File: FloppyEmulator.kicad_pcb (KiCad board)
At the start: 2 copper layers, 69.9 x 48.3 mm, 48 parts, among them Q1 Crystal_GND24, Q2 BC817, Q3 BC817, SW1 ALPS_5WAY, U1 STM32F405RGTx, U10 AP1117-15, U2 SN74LVC2G07, U3 SN74LVC2G07, U4 SN74LVC2G07, U5 SN74LVC2G07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

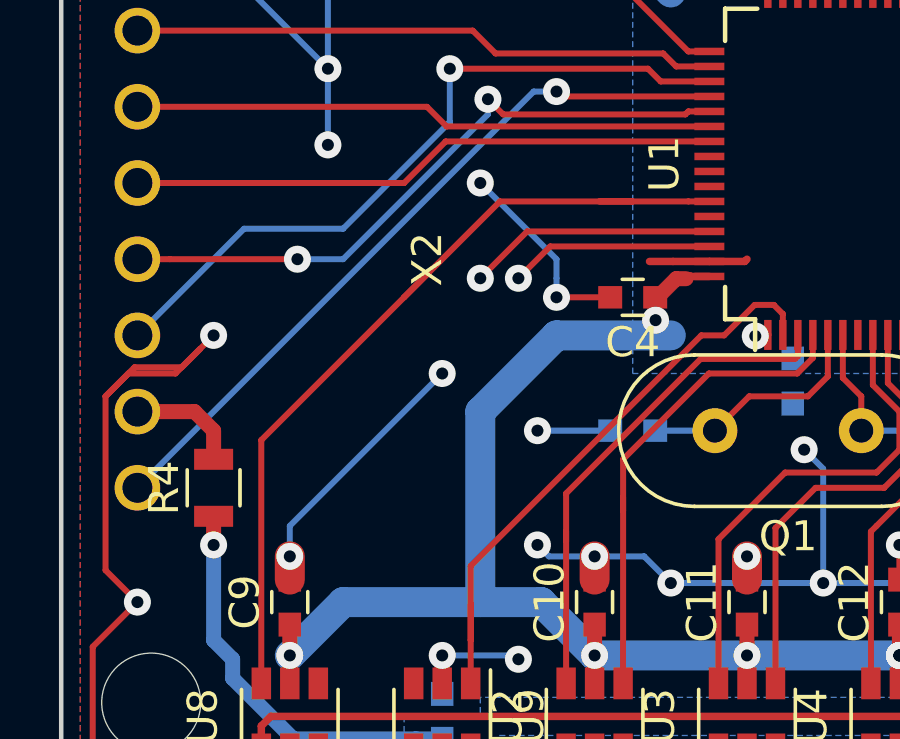
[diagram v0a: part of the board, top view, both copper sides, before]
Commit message: Add I2C pullups
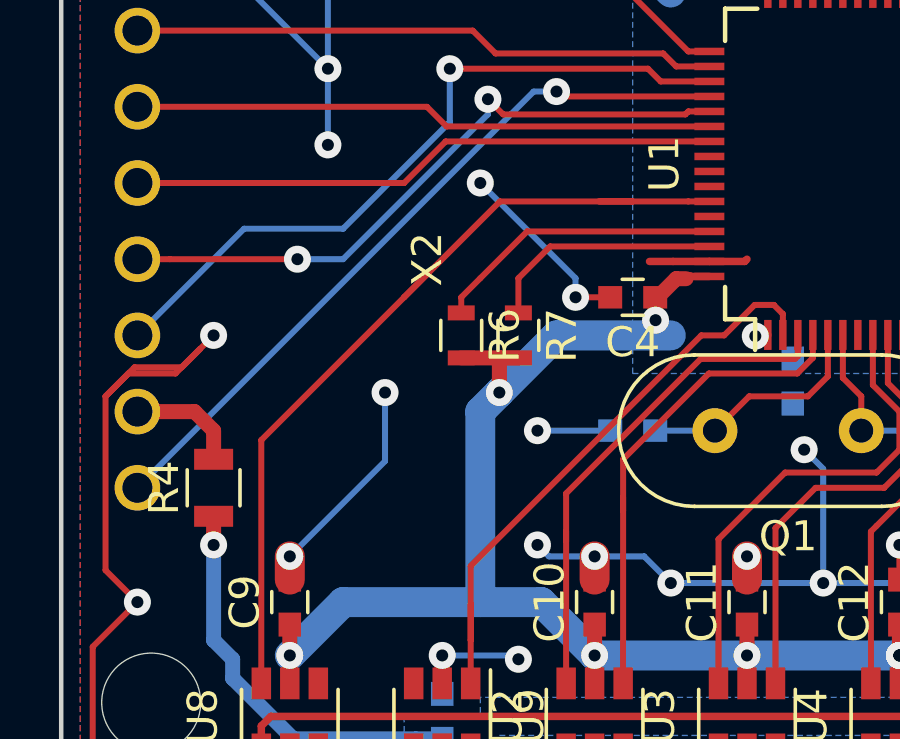
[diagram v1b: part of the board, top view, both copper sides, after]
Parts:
- added R6: DNF, Resistors_SMD:R_0603, F.Cu at (153.0, 82.5)
- added R7: DNF, Resistors_SMD:R_0603, F.Cu at (154.9, 82.5)
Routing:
- net +3V3: track 147.0 -> 150.1 mm, vias 24 -> 25
- net GND: track 374.6 -> 372.8 mm
- net SCL: track 8.28 -> 9.70 mm, vias 1 -> 0
- net SDA: track 6.80 -> 7.96 mm, vias 1 -> 0
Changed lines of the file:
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@@
     (thickness 1.6)
     (drawings 6)
-    (tracks 656)
+    (tracks 662)
     (zones 0)
-    (modules 48)
+    (modules 50)
     (nets 92)
   )
@@
   )
   (setup
-    (last_trace_width 0.2)
+    (last_trace_width 0.5)
     (user_trace_width 0.2)
     (user_trace_width 0.25)
@@
     )
   )
+  (module Resistors_SMD:R_0603 (layer F.Cu)
+    (at 153.035 82.55 270)
+    (descr "Resistor SMD 0603, reflow soldering, Vishay (see dcrcw.pdf)")
+    (tags "resistor 0603")
+    (attr smd)
+    (fp_text reference R6 (at 0 -1.45 270) (layer F.SilkS)
+      (effects (font (size 1 1) (thickness 0.15)))
+    )
+    (fp_text value DNF (at 0 1.5 270) (layer F.Fab)
+      (effects (font (size 1 1) (thickness 0.15)))
+    )
+    (fp_line (start 1.25 0.7) (end -1.25 0.7) (layer F.CrtYd) (width 0.05))
+    (fp_line (start 1.25 0.7) (end 1.25 -0.7) (layer F.CrtYd) (width 0.05))
+    (fp_line (start -1.25 -0.7) (end -1.25 0.7) (layer F.CrtYd) (width 0.05))
+    (fp_line (start -1.25 -0.7) (end 1.25 -0.7) (layer F.CrtYd) (width 0.05))
+    (fp_line (start -0.5 -0.68) (end 0.5 -0.68) (layer F.SilkS) (width 0.12))
+    (fp_line (start 0.5 0.68) (end -0.5 0.68) (layer F.SilkS) (width 0.12))
+    (fp_line (start -0.8 -0.4) (end 0.8 -0.4) (layer F.Fab) (width 0.1))
+    (fp_line (start 0.8 -0.4) (end 0.8 0.4) (layer F.Fab) (width 0.1))
+    (fp_line (start 0.8 0.4) (end -0.8 0.4) (layer F.Fab) (width 0.1))
+    (fp_line (start -0.8 0.4) (end -0.8 -0.4) (layer F.Fab) (width 0.1))
+    (fp_text user %R (at 0 0 270) (layer F.Fab)
+      (effects (font (size 0.4 0.4) (thickness 0.075)))
+    )
+    (pad 2 smd rect (at 0.75 0 270) (size 0.5 0.9) (layers F.Cu F.Paste F.Mask)
+      (net 9 +3V3))
+    (pad 1 smd rect (at -0.75 0 270) (size 0.5 0.9) (layers F.Cu F.Paste F.Mask)
+      (net 11 SCL))
+    (model ${KISYS3DMOD}/Resistors_SMD.3dshapes/R_0603.wrl
+      (at (xyz 0 0 0))
+      (scale (xyz 1 1 1))
+      (rotate (xyz 0 0 0))
+    )
+  )
+  (module Resistors_SMD:R_0603 (layer F.Cu)
+    (at 154.94 82.55 270)
+    (descr "Resistor SMD 0603, reflow soldering, Vishay (see dcrcw.pdf)")
+    (tags "resistor 0603")
+    (attr smd)
+    (fp_text reference R7 (at 0 -1.45 270) (layer F.SilkS)
+      (effects (font (size 1 1) (thickness 0.15)))
+    )
+    (fp_text value DNF (at 0 1.5 270) (layer F.Fab)
+      (effects (font (size 1 1) (thickness 0.15)))
+    )
+    (fp_text user %R (at 0 0 270) (layer F.Fab)
+      (effects (font (size 0.4 0.4) (thickness 0.075)))
+    )
+    (fp_line (start -0.8 0.4) (end -0.8 -0.4) (layer F.Fab) (width 0.1))
+    (fp_line (start 0.8 0.4) (end -0.8 0.4) (layer F.Fab) (width 0.1))
+    (fp_line (start 0.8 -0.4) (end 0.8 0.4) (layer F.Fab) (width 0.1))
+    (fp_line (start -0.8 -0.4) (end 0.8 -0.4) (layer F.Fab) (width 0.1))
+    (fp_line (start 0.5 0.68) (end -0.5 0.68) (layer F.SilkS) (width 0.12))
+    (fp_line (start -0.5 -0.68) (end 0.5 -0.68) (layer F.SilkS) (width 0.12))
+    (fp_line (start -1.25 -0.7) (end 1.25 -0.7) (layer F.CrtYd) (width 0.05))
+    (fp_line (start -1.25 -0.7) (end -1.25 0.7) (layer F.CrtYd) (width 0.05))
+    (fp_line (start 1.25 0.7) (end 1.25 -0.7) (layer F.CrtYd) (width 0.05))
+    (fp_line (start 1.25 0.7) (end -1.25 0.7) (layer F.CrtYd) (width 0.05))
+    (pad 1 smd rect (at -0.75 0 270) (size 0.5 0.9) (layers F.Cu F.Paste F.Mask)
+      (net 10 SDA))
+    (pad 2 smd rect (at 0.75 0 270) (size 0.5 0.9) (layers F.Cu F.Paste F.Mask)
+      (net 9 +3V3))
+    (model ${KISYS3DMOD}/Resistors_SMD.3dshapes/R_0603.wrl
+      (at (xyz 0 0 0))
+      (scale (xyz 1 1 1))
+      (rotate (xyz 0 0 0))
+    )
+  )
   (dimension 48.26 (width 0.3) (layer F.SilkS)
     (gr_text "48.260 mm" (at 217.25 81.28 270) (layer F.SilkS)
@@
   (segment (start 159.766 73.152) (end 160.199 73.585) (width 0.2) (layer F.Cu) (net 7))
   (segment (start 160.199 73.585) (end 161.305 73.585) (width 0.2) (layer F.Cu) (net 7))
+  (segment (start 153.67 77.47) (end 156.845 80.645) (width 0.2) (layer B.Cu) (net 8))
+  (segment (start 158 81.28) (end 156.845 81.28) (width 0.2) (layer F.Cu) (net 8))
+  (segment (start 156.845 80.645) (end 156.845 81.28) (width 0.2) (layer B.Cu) (net 8))
+  (via (at 156.845 81.28) (size 0.9) (drill 0.4) (layers F.Cu B.Cu) (net 8))
+  (segment (start 150.495 86.741) (end 150.495 85.091396) (width 0.2) (layer B.Cu) (net 8))
+  (segment (start 147.32 89.916) (end 150.495 86.741) (width 0.2) (layer B.Cu) (net 8))
+  (segment (start 150.495 85.091396) (end 150.495 84.455) (width 0.2) (layer B.Cu) (net 8))
+  (via (at 150.495 84.455) (size 0.9) (drill 0.4) (layers F.Cu B.Cu) (net 8))
   (segment (start 160.095 80.085) (end 159.31 80.085) (width 0.25) (layer F.Cu) (net 8))
-  (segment (start 153.67 77.47) (end 156.21 80.01) (width 0.2) (layer B.Cu) (net 8))
-  (segment (start 156.21 80.01) (end 156.21 80.643604) (width 0.2) (layer B.Cu) (net 8))
-  (segment (start 158 81.28) (end 156.21 81.28) (width 0.2) (layer F.Cu) (net 8))
-  (segment (start 156.21 80.643604) (end 156.21 81.28) (width 0.2) (layer B.Cu) (net 8))
-  (via (at 156.21 81.28) (size 0.9) (drill 0.4) (layers F.Cu B.Cu) (net 8))
   (via (at 153.67 77.47) (size 0.9) (drill 0.4) (layers F.Cu B.Cu) (net 8))
   (segment (start 204.47 80.632436) (end 204.47 78.74) (width 0.2) (layer B.Cu) (net 8))
@@
   (segment (start 141.177999 84.580239) (end 142.146237 83.612001) (width 0.2) (layer F.Cu) (net 8))
   (segment (start 141.938238 83.82) (end 143.51 83.82) (width 0.2) (layer F.Cu) (net 8))
-  (segment (start 147.32 88.9) (end 152.4 83.82) (width 0.2) (layer B.Cu) (net 8))
-  (segment (start 147.32 89.916) (end 147.32 88.9) (width 0.2) (layer B.Cu) (net 8))
-  (via (at 152.4 83.82) (size 0.9) (drill 0.4) (layers F.Cu B.Cu) (net 8))
   (segment (start 140.749999 97.569999) (end 140.749999 92.930001) (width 0.2) (layer F.Cu) (net 8))
   (segment (start 142.24 99.06) (end 140.749999 97.569999) (width 0.2) (layer F.Cu) (net 8))
@@
   (segment (start 172.72 96.35) (end 172.72 97.282) (width 0.5) (layer F.Cu) (net 8))
   (via (at 172.72 97.282) (size 0.9) (drill 0.4) (layers F.Cu B.Cu) (net 8))
+  (segment (start 154.305 83.3) (end 154.94 83.3) (width 0.5) (layer F.Cu) (net 9))
+  (segment (start 153.035 83.3) (end 154.305 83.3) (width 0.5) (layer F.Cu) (net 9))
+  (segment (start 154.305 84.455) (end 154.305 83.3) (width 0.5) (layer F.Cu) (net 9))
+  (segment (start 154.305 84.455) (end 156.21 82.55) (width 1) (layer B.Cu) (net 9))
+  (segment (start 153.67 85.09) (end 154.305 84.455) (width 1) (layer B.Cu) (net 9))
+  (via (at 154.305 84.455) (size 0.9) (drill 0.4) (layers F.Cu B.Cu) (net 9))
   (segment (start 184.15 78.74) (end 184.15 80.01) (width 0.25) (layer F.Cu) (net 9))
   (via (at 184.15 80.01) (size 0.9) (drill 0.4) (layers F.Cu B.Cu) (net 9))
@@
   (segment (start 169.255 82.535) (end 169.255 81.282953) (width 0.25) (layer F.Cu) (net 9))
   (via (at 168.640545 80.668498) (size 0.9) (drill 0.4) (layers F.Cu B.Cu) (net 9))
+  (segment (start 154.94 80.645) (end 154.94 81.8) (width 0.2) (layer F.Cu) (net 10))
   (segment (start 156 79.585) (end 154.94 80.645) (width 0.2) (layer F.Cu) (net 10))
   (segment (start 161.305 79.585) (end 156 79.585) (width 0.2) (layer F.Cu) (net 10))
-  (via (at 154.94 80.645) (size 0.9) (drill 0.4) (layers F.Cu B.Cu) (net 10))
+  (segment (start 153.035 81.8) (end 153.035 81.28) (width 0.2) (layer F.Cu) (net 11))
+  (segment (start 153.035 81.28) (end 153.67 80.645) (width 0.2) (layer F.Cu) (net 11))
   (segment (start 155.23 79.085) (end 153.67 80.645) (width 0.2) (layer F.Cu) (net 11))
   (segment (start 161.305 79.085) (end 155.23 79.085) (width 0.2) (layer F.Cu) (net 11))
-  (via (at 153.67 80.645) (size 0.9) (drill 0.4) (layers F.Cu B.Cu) (net 11))
   (segment (start 151.13 81.28) (end 154.325 78.085) (width 0.2) (layer F.Cu) (net 39))
   (segment (start 154.325 78.085) (end 158.75 78.085) (width 0.2) (layer F.Cu) (net 39))
@@
   (segment (start 163.83 67.693) (end 162.802 66.665) (width 0.25) (layer F.Cu) (net 80))
   (segment (start 163.755 70.417186) (end 163.83 70.342186) (width 0.25) (layer F.Cu) (net 80))
-  (segment (start 153.67 85.09) (end 156.21 82.55) (width 1) (layer B.Cu) (net 9))
   (segment (start 153.67 91.44) (end 153.67 85.09) (width 1) (layer B.Cu) (net 9))
   (segment (start 156.21 82.55) (end 160.02 82.55) (width 1) (layer B.Cu) (net 9))

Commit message: Cleanups
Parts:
- added C23: 10u, Capacitors_SMD:C_1210, F.Cu at (146.7, 67.3)
- added C24: 10u, Capacitors_SMD:C_1210, B.Cu at (165.1, 74.9)
- moved C8 12.3 mm to (156.2, 64.1)
- moved C21 1.27 mm to (175.0, 71.4), turned to 270 degrees
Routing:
- net GND: track 372.8 -> 399.8 mm, vias 80 -> 88
- net +3V3: track 150.1 -> 153.4 mm
- net SPI1_NSS: track 22.4 -> 23.7 mm
- net +5VDC: track 28.3 -> 29.2 mm
- net /BUTTON4: track 39.9 -> 39.4 mm

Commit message: Credits
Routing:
- net GND: track 399.8 -> 390.6 mm, vias 88 -> 85
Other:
- board text added: "Yet Another Floppy Emulator"
- board text added: "tnt23/2018"
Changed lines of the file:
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@@
   (general
     (thickness 1.6)
-    (drawings 6)
-    (tracks 687)
+    (drawings 10)
+    (tracks 682)
     (zones 0)
     (modules 52)
@@
   )
   (setup
-    (last_trace_width 0.8)
+    (last_trace_width 0.2)
     (user_trace_width 0.2)
     (user_trace_width 0.25)
@@
     )
   )
+  (gr_poly (pts (xy 207.772 98.552) (xy 207.772 100.584) (xy 196.342 100.584) (xy 196.342 98.552)) (layer B.Mask) (width 0.15))
+  (gr_poly (pts (xy 207.772 69.596) (xy 207.772 77.724) (xy 198.882 77.724) (xy 198.882 69.596)) (layer B.Mask) (width 0.15))
+  (gr_text tnt23/2018 (at 207.772 99.568) (layer B.Cu)
+    (effects (font (size 1.27 1.27) (thickness 0.2)) (justify left mirror))
+  )
+  (gr_text "Yet\nAnother\nFloppy\nEmulator" (at 207.645 73.66) (layer B.Cu)
+    (effects (font (size 1.27 1.27) (thickness 0.2)) (justify left mirror))
+  )
   (dimension 48.26 (width 0.3) (layer F.SilkS)
     (gr_text "48.260 mm" (at 217.25 81.28 270) (layer F.SilkS)
@@
   (segment (start 156.972 73.152) (end 157.405 73.585) (width 0.2) (layer F.Cu) (net 7))
   (segment (start 157.405 73.585) (end 161.305 73.585) (width 0.2) (layer F.Cu) (net 7))
+  (segment (start 201.93 67.945) (end 205.105 67.945) (width 0.5) (layer B.Cu) (net 8))
+  (via (at 205.105 67.945) (size 0.9) (drill 0.4) (layers F.Cu B.Cu) (net 8))
+  (segment (start 201.295 67.945) (end 201.93 67.945) (width 0.5) (layer B.Cu) (net 8))
+  (segment (start 196.85 63.5) (end 201.295 67.945) (width 0.5) (layer B.Cu) (net 8))
+  (via (at 201.93 67.945) (size 0.9) (drill 0.4) (layers F.Cu B.Cu) (net 8))
   (segment (start 163.576 76.454) (end 163.576 74.954) (width 1) (layer B.Cu) (net 8))
   (segment (start 163.576 74.954) (end 163.6 74.93) (width 1) (layer B.Cu) (net 8))
@@
   (segment (start 177.800006 81.914994) (end 178.435 81.914994) (width 0.2) (layer F.Cu) (net 8))
   (via (at 178.435 81.914994) (size 0.9) (drill 0.4) (layers F.Cu B.Cu) (net 8))
-  (segment (start 199.39 66.04) (end 198.628 65.278) (width 0.2) (layer B.Cu) (net 8))
   (segment (start 182.88 60.96) (end 187.198 65.278) (width 0.2) (layer B.Cu) (net 8))
   (segment (start 191.12 65.39) (end 191.008 65.278) (width 0.5) (layer F.Cu) (net 8))
@@
   (segment (start 191.644396 65.278) (end 191.008 65.278) (width 0.2) (layer B.Cu) (net 8))
   (segment (start 191.516 65.278) (end 191.008 65.278) (width 0.5) (layer F.Cu) (net 8))
-  (segment (start 198.628 65.278) (end 191.644396 65.278) (width 0.2) (layer B.Cu) (net 8))
   (segment (start 191.628 65.39) (end 191.516 65.278) (width 0.5) (layer F.Cu) (net 8))
   (via (at 191.008 65.278) (size 0.9) (drill 0.4) (layers F.Cu B.Cu) (net 8))
@@
   (segment (start 199.39 71.12) (end 198.12 69.85) (width 0.2) (layer F.Cu) (net 8))
   (segment (start 201.93 71.12) (end 199.39 71.12) (width 0.2) (layer F.Cu) (net 8))
-  (via (at 198.12 69.85) (size 0.9) (drill 0.4) (layers F.Cu B.Cu) (net 8))
   (segment (start 199.39 68.58) (end 201.93 71.12) (width 0.2) (layer F.Cu) (net 8))
-  (via (at 201.93 71.12) (size 0.9) (drill 0.4) (layers F.Cu B.Cu) (net 8))
   (segment (start 199.39 66.04) (end 199.39 68.58) (width 0.2) (layer F.Cu) (net 8))
   (segment (start 199.39 66.04) (end 196.85 63.5) (width 0.2) (layer F.Cu) (net 8))
   (via (at 196.85 63.5) (size 0.9) (drill 0.4) (layers F.Cu B.Cu) (net 8))
-  (via (at 199.39 66.04) (size 0.9) (drill 0.4) (layers F.Cu B.Cu) (net 8))
   (segment (start 194.408 68.99) (end 194.564 68.834) (width 0.2) (layer F.Cu) (net 8))
   (segment (start 192.79 68.99) (end 194.408 68.99) (width 0.2) (layer F.Cu) (net 8))
@@
   (segment (start 205.74 101.6) (end 200.66 101.6) (width 0.2) (layer B.Cu) (net 8))
   (via (at 200.66 101.6) (size 0.9) (drill 0.4) (layers F.Cu B.Cu) (net 8))
-  (segment (start 203.2 99.06) (end 205.74 101.6) (width 0.2) (layer B.Cu) (net 8))
-  (segment (start 203.2 96.52) (end 203.2 99.06) (width 0.2) (layer B.Cu) (net 8))
   (via (at 205.74 101.6) (size 0.9) (drill 0.4) (layers F.Cu B.Cu) (net 8))
   (segment (start 203.2 93.98) (end 203.2 96.52) (width 0.2) (layer B.Cu) (net 8))
@@
   (via (at 205.74 91.44) (size 0.9) (drill 0.4) (layers F.Cu B.Cu) (net 8))
   (segment (start 206.275914 90.904086) (end 205.74 91.44) (width 0.2) (layer B.Cu) (net 8))
-  (segment (start 205.74 73.66) (end 205.74 68.58) (width 0.2) (layer B.Cu) (net 8))
-  (via (at 205.74 68.58) (size 0.9) (drill 0.4) (layers F.Cu B.Cu) (net 8))
   (segment (start 207.54 75.46) (end 205.74 73.66) (width 0.2) (layer F.Cu) (net 8))
   (segment (start 207.54 78.34) (end 207.54 75.46) (width 0.2) (layer F.Cu) (net 8))
-  (via (at 205.74 73.66) (size 0.9) (drill 0.4) (layers F.Cu B.Cu) (net 8))
   (segment (start 187.96 60.96) (end 203.2 60.96) (width 0.2) (layer B.Cu) (net 8))
   (via (at 203.2 60.96) (size 0.9) (drill 0.4) (layers F.Cu B.Cu) (net 8))
